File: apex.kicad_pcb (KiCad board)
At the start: 4 copper layers, 65.4 x 30.5 mm, 45 parts, among them J1 Conn_01x04_Pin, J2 USB_C_Receptacle_USB2.0_16P, J3 Conn_01x04_Pin, J5 Conn_01x04_Pin, SW1 PCM12SMTR, SW2 KMR223G LFG, U1 AP7363-33D-13, U2 APX803L20-29SA-7, U4 STM32F070RBTx, U7 USBLC6-2P6, Y2 XRCGB32M000F2P01R0

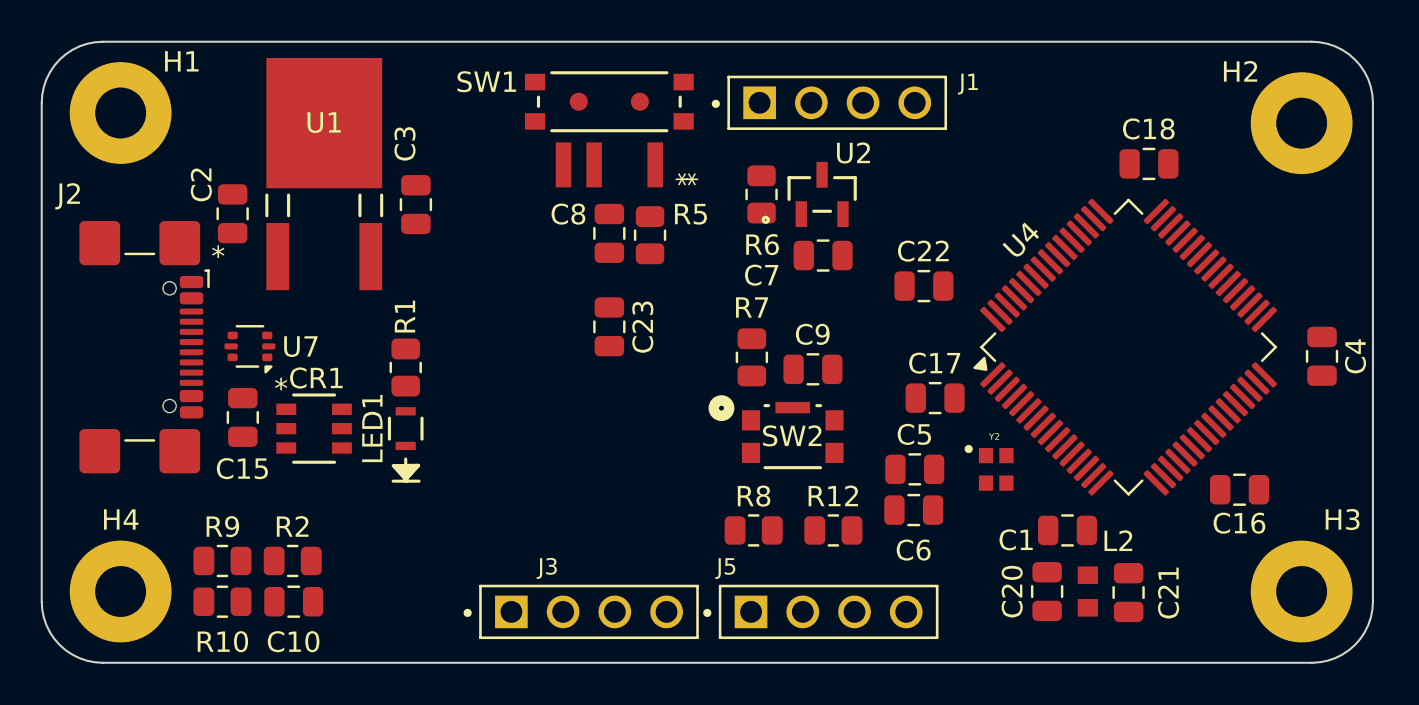
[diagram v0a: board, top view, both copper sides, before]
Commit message: matched footprint name to name of component
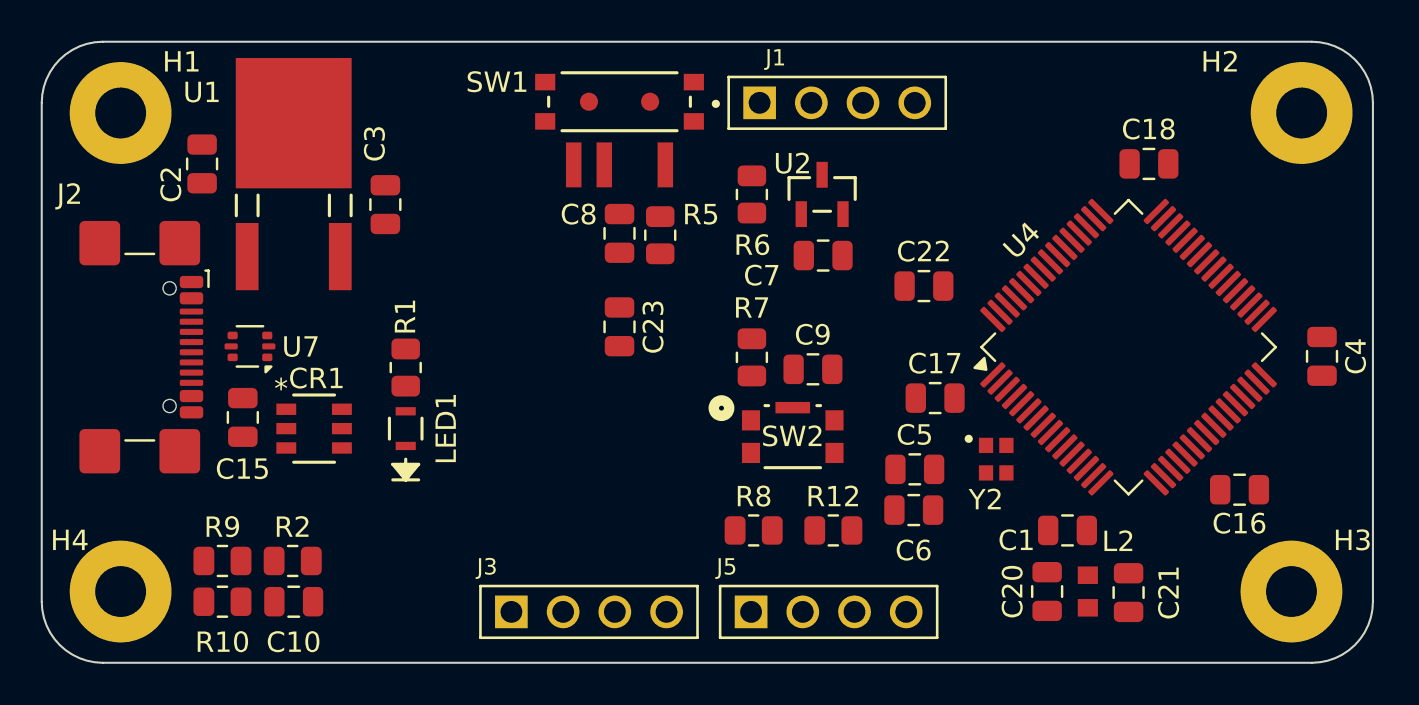
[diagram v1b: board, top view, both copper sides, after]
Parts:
- J1: footprint PPTC041LFBN_RC:SULLINS_PPTC041LFBN-RC -> PPTC041LFBN_RC:PPTC041LFBN-RC
- LED1: footprint 150080BS75000:LED_BS75000_WRE -> 150080BS75000:150080BS75000
- U1: footprint AP7363_33D_13:TO252-3L_DIO -> AP7363_33D_13:AP7363-33D-13
- U2: footprint APX803L20-29-SA-7:SOT23_SA_DIO -> APX803L20-29-SA-7:APX803L20-29SA-7
- moved C2 2.87 mm to (24.5, 37.0)
- moved C3 1.50 mm to (33.5, 39.0)
- moved U1 1.50 mm to (29.0, 35.0)
- moved C23 0.50 mm to (45.0, 45.0)
- moved C8 0.50 mm to (45.0, 40.4)
- moved H2 0.50 mm to (78.5, 34.5)
- moved H3 0.50 mm to (78.0, 58.0)
- moved R5 0.50 mm to (47.0, 40.5)
- moved SW1 0.50 mm to (45.0, 33.9)
- moved Y2 0.50 mm to (63.5, 51.5)
- moved R6 0.47 mm to (51.5, 38.5)

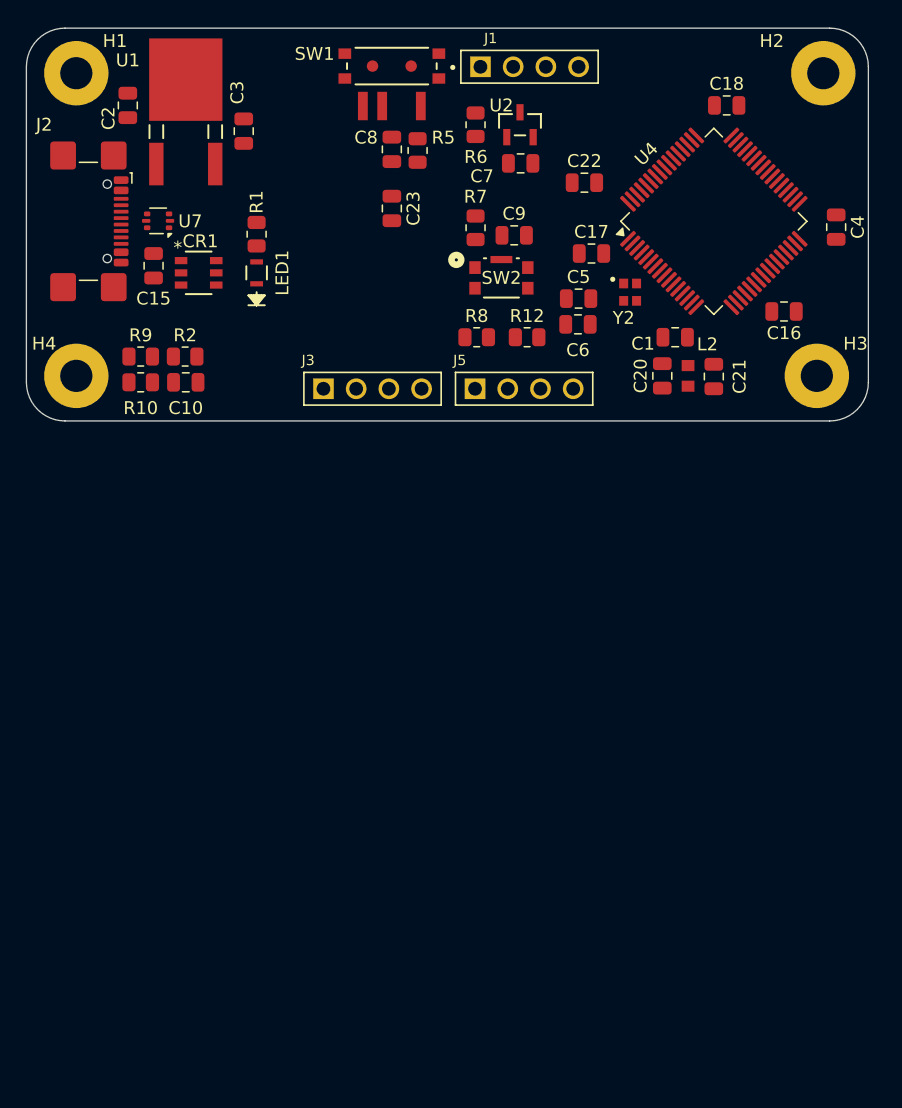
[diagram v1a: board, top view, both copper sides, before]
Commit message: updating pcb
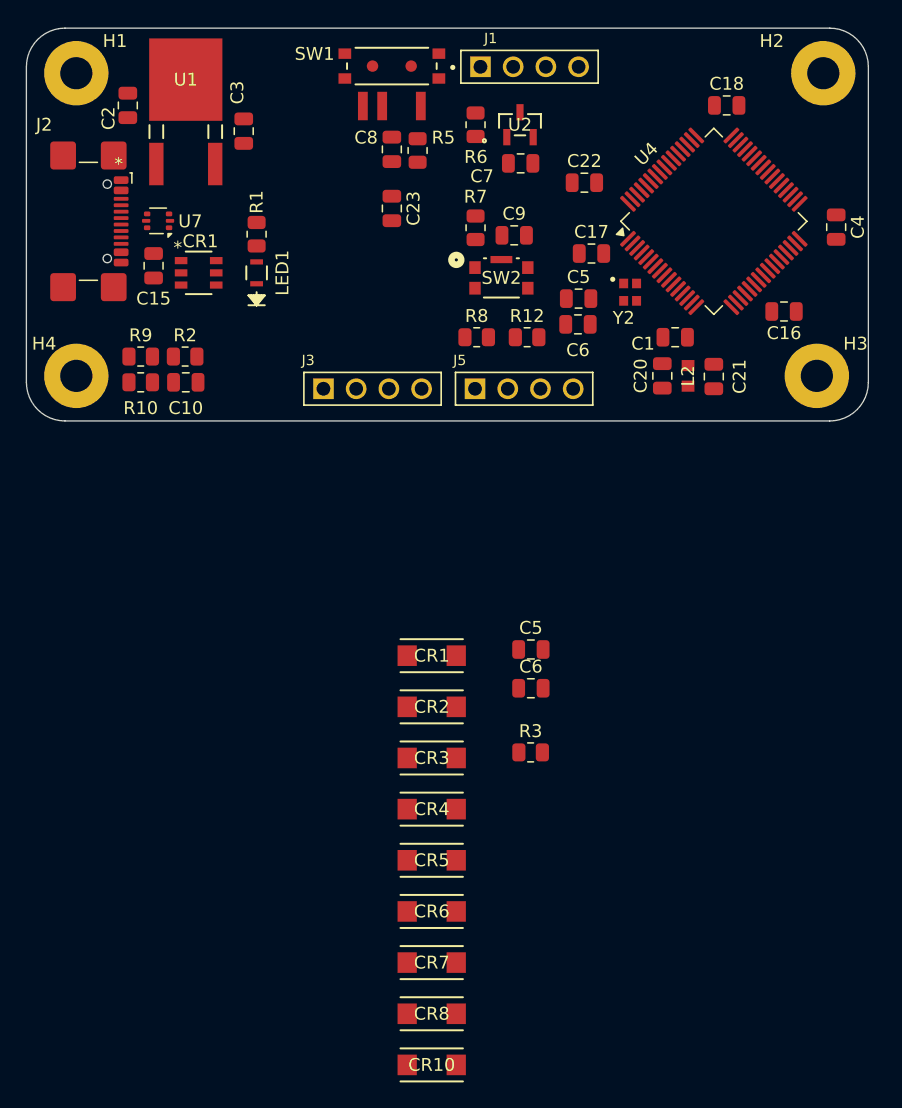
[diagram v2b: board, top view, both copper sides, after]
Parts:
- added C5: C, Capacitor_SMD:C_0805_2012Metric, F.Cu at (55.8, 79.2)
- added C6: C, Capacitor_SMD:C_0805_2012Metric, F.Cu at (55.8, 82.3)
- added CR1: SD2010S040S3R0, DIODE_SCHOTTKY_40V_3A:SDO_KAVX_KAV, F.Cu at (48.1, 79.7)
- added CR10: SD2010S040S3R0, DIODE_SCHOTTKY_40V_3A:SDO_KAVX_KAV, F.Cu at (48.1, 111.5)
- added CR2: SD2010S040S3R0, DIODE_SCHOTTKY_40V_3A:SDO_KAVX_KAV, F.Cu at (48.1, 83.7)
- added CR3: SD2010S040S3R0, DIODE_SCHOTTKY_40V_3A:SDO_KAVX_KAV, F.Cu at (48.1, 87.7)
- added CR4: SD2010S040S3R0, DIODE_SCHOTTKY_40V_3A:SDO_KAVX_KAV, F.Cu at (48.1, 91.6)
- added CR5: SD2010S040S3R0, DIODE_SCHOTTKY_40V_3A:SDO_KAVX_KAV, F.Cu at (48.1, 95.6)
- added CR6: SD2010S040S3R0, DIODE_SCHOTTKY_40V_3A:SDO_KAVX_KAV, F.Cu at (48.1, 99.6)
- added CR7: SD2010S040S3R0, DIODE_SCHOTTKY_40V_3A:SDO_KAVX_KAV, F.Cu at (48.1, 103.6)
- added CR8: SD2010S040S3R0, DIODE_SCHOTTKY_40V_3A:SDO_KAVX_KAV, F.Cu at (48.1, 107.5)
- added R3: 10k, Resistor_SMD:R_0805_2012Metric, F.Cu at (55.8, 87.2)
- C1: value 10 nF -> C
- C10: value 0.1 uF -> C
- C15, C16, C17, C18, C22, C4, C7: value 100 nF -> C
- C2, C23, C3: value 10 uF -> C
- C20, C21: value 1 uF -> C
- H1: value H1_MH -> MountingHole
- H2: value H2_MH -> MountingHole
- H3: value H3_MH -> MountingHole
- H4: value H4_MH -> MountingHole
- L2: footprint MH1608:IND_BOURNS_MH1608 -> FERR_0603_120:IND_BOURNS_MH1608
- R1: value 3.3 -> R
- R10, R9: value 5.1k -> R
- R12, R8: value 1 K -> R
- R2: value 330 -> R
- R6: value 100K -> R
- U1: footprint AP7363_33D_13:AP7363-33D-13 -> PMIC_VREG_LDO_3.3V:TO252-3L_DIO
- U2: footprint APX803L20-29-SA-7:APX803L20-29SA-7 -> PMIC_SUPERVISOR_1CH:SOT23_SA_DIO
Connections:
- net +3.3 VA renamed +3.3VA
- C16 pad 2: +3.3 V -> VDD
- C17 pad 2: +3.3 V -> VDD
- C18 pad 2: +3.3 V -> VDD
- C2 pad 2: VBUS -> +5V
- C21 pad 2: +3.3 V -> VDD
- C22 pad 2: +3.3 V -> VDD
- C23 pad 2: +3.3 V -> VDD
- C3 pad 2: +3.3 V -> +3V3
- C4 pad 2: +3.3 V -> VDD
- C7 pad 1: GND -> GND2
- C7 pad 2: +3.3 V -> VPP
- J1 pad 1: +3.3 V -> +3V3
- J3 pad 1: +3.3 V -> +3V3
- J5 pad 1: +3.3 V -> +3V3
- L2 pad 1: +3.3 V -> VDD
- R1 pad 2: +3.3 V -> VCC
- R12 pad 1: +3.3 V -> +3V3
- R6 pad 1: +3.3 V -> VPP
- R6 pad 2: NRST -> RST_L
- R8 pad 1: +3.3 V -> +3V3
- U1 pad 1: VBUS -> +5V
- U1 pad 3: +3.3 V -> +3V3
- U2 pad 1: +3.3 V -> VPP
- U2 pad 2: GND -> GND2
- U2 pad 3: NRST -> RST_L
- U4 pad 1: +3.3 V -> VDD
- U4 pad 19: +3.3 V -> VDD
- U4 pad 32: +3.3 V -> VDD
- U4 pad 41: unconnected-(U4-PA8-Pad41) -> USART1_TX
- U4 pad 42: USART1_TX -> USART1_RX
- U4 pad 43: USART1_RX -> USB_N
- U4 pad 44: USB_N -> USB_P
- U4 pad 45: USB_P -> SWDIO
- U4 pad 46: SWDIO -> SWCLK
- U4 pad 48: +3.3 V -> VDD
- U4 pad 49: SWCLK -> unconnected-(U4-PA14-Pad49)
- U4 pad 5: HSE_IN -> CLK_32MHZ
- U4 pad 6: HSE_OUT -> unconnected-(U4-PF1-Pad6)
- U4 pad 60: Boot0 -> Net-(U4-BOOT0)
- U4 pad 64: +3.3 V -> VDD
- U4 pad 7: NRST -> RST_L

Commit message: added sheets
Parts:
- removed the C5 at (59.5, 52.0)
- removed the C6 at (59.5, 54.0)
- removed C8: 100 nF, Capacitor_SMD:C_0805_2012Metric
- removed C9: 47 nF, Capacitor_SMD:C_0805_2012Metric
- removed the CR1 at (30.0, 50.0)
- removed R5: 10K, Resistor_SMD:R_0805_2012Metric
- removed R7: 100K, Resistor_SMD:R_0805_2012Metric
- removed SW1: PCM12SMTR, PCM12SMTR:PCM12SMTR_CNK
- removed SW2: KMR223G LFG, KMR223_LFG:KMR2_G_CNK
- added U5: ~, Package_SO:SOIC-8-1EP_3.9x4.9mm_P1.27mm_EP2.41x3.3mm, F.Cu at (50.8, 48.6)
- J1: footprint PPTC041LFBN_RC:PPTC041LFBN-RC -> J_1x4:PPTC041LFBN-RC
- J3, J5: footprint PPTC041LFBN_RC:SULLINS_PPTC041LFBN-RC -> J_1x4:PPTC041LFBN-RC
- LED1: footprint 150080BS75000:150080BS75000 -> LED_0805_BLUE:150080BS75000
- Y2: footprint XRCGB32M000F2P01R0:OSC_XRCGB32M000F2P01R0 -> CRYSTAL_32MHZ:OSC_XRCGB32M000F2P01R0
- moved CR8 73.5 mm to (48.1, 34.0)
- moved CR5 57.3 mm to (39.5, 39.0), turned to -90 degrees
- moved CR10 56.3 mm to (42.0, 55.5)
- moved CR4 56.2 mm to (27.0, 39.5), turned to -90 degrees
- moved R3 56.1 mm to (72.0, 33.5)
- moved CR7 54.6 mm to (35.4, 50.5), turned to 180 degrees
- moved CR6 53.6 mm to (35.5, 47.5), turned to 180 degrees
- moved CR2 42.3 mm to (36.5, 43.0), turned to 90 degrees
- moved C6 37.3 mm to (46.4, 46.2)
- moved CR3 36.4 mm to (35.5, 53.5), turned to 180 degrees
- moved C5 29.6 mm to (46.3, 51.2)
- moved CR1 24.2 mm to (48.0, 55.5)
- moved Y2 16.9 mm to (46.9, 48.7)
- moved C7 13.0 mm to (43.0, 36.5)
- moved R6 13.0 mm to (39.5, 33.5)
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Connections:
- C5 pad 1: GND1 -> GND
- C6 pad 1: GND1 -> GND
- C7 pad 1: GND2 -> GND
- R3 pad 1: Net-(U4-BOOT0) -> Boot0
- U2 pad 2: GND2 -> GND
- U4 pad 60: Net-(U4-BOOT0) -> Boot0
- Y2 pad 1: HSE_IN -> XIN
- Y2 pad 3: HSE_OUT -> XOUT
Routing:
- net GND: track 0.00 -> 266.1 mm, vias 0 -> 26
- net VDD: track 0.00 -> 109.5 mm, vias 0 -> 13
- net USB_N: track 0.00 -> 52.7 mm, vias 0 -> 5
- net USB_P: track 0.00 -> 51.3 mm, vias 0 -> 5
- net GNDPWR: track 0.00 -> 42.4 mm, vias 0 -> 3
- net RST_L: track 0.00 -> 41.3 mm, vias 0 -> 2
- net VDC: track 0.00 -> 39.0 mm, vias 0 -> 3
- net +3V3: track 0.00 -> 32.8 mm
- net I2C2_SCL: track 0.00 -> 31.0 mm, vias 0 -> 2
- net I2C2_SDA: track 0.00 -> 28.2 mm, vias 0 -> 2
- net CLK_32MHZ: track 0.00 -> 20.5 mm, vias 0 -> 2
- net USB_CC1: track 0.00 -> 19.0 mm, vias 0 -> 2
- net VBUS: track 0.00 -> 15.5 mm, vias 0 -> 3
- net +3.3VA: track 0.00 -> 15.1 mm, vias 0 -> 2
- net USB_CC2: track 0.00 -> 11.4 mm, vias 0 -> 2
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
